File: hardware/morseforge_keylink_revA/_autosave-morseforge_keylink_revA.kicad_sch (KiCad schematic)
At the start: 18 parts, among them J1 USB_C_Receptacle_USB2.0_14P, J2 Conn_01x02_Socket, SW1 SW_SPST, U1 MCP73831-2-MC, U2 LDO40LPU33RY

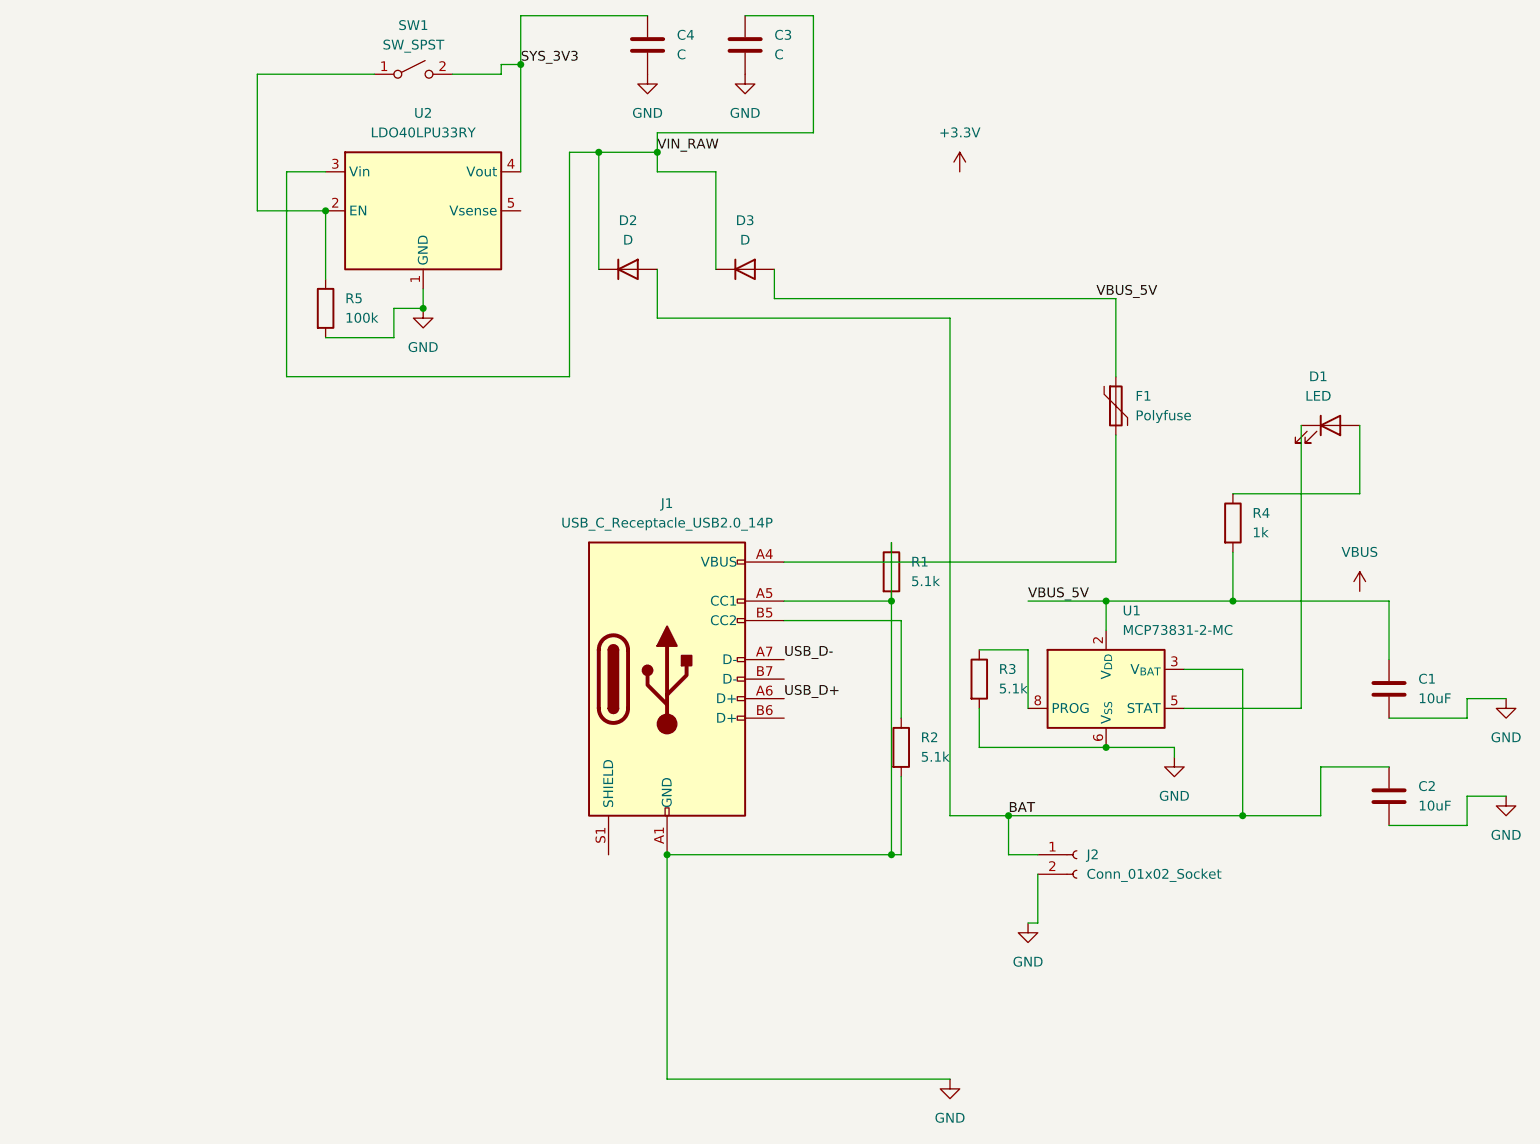
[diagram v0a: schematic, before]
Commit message: USB-UART blocks
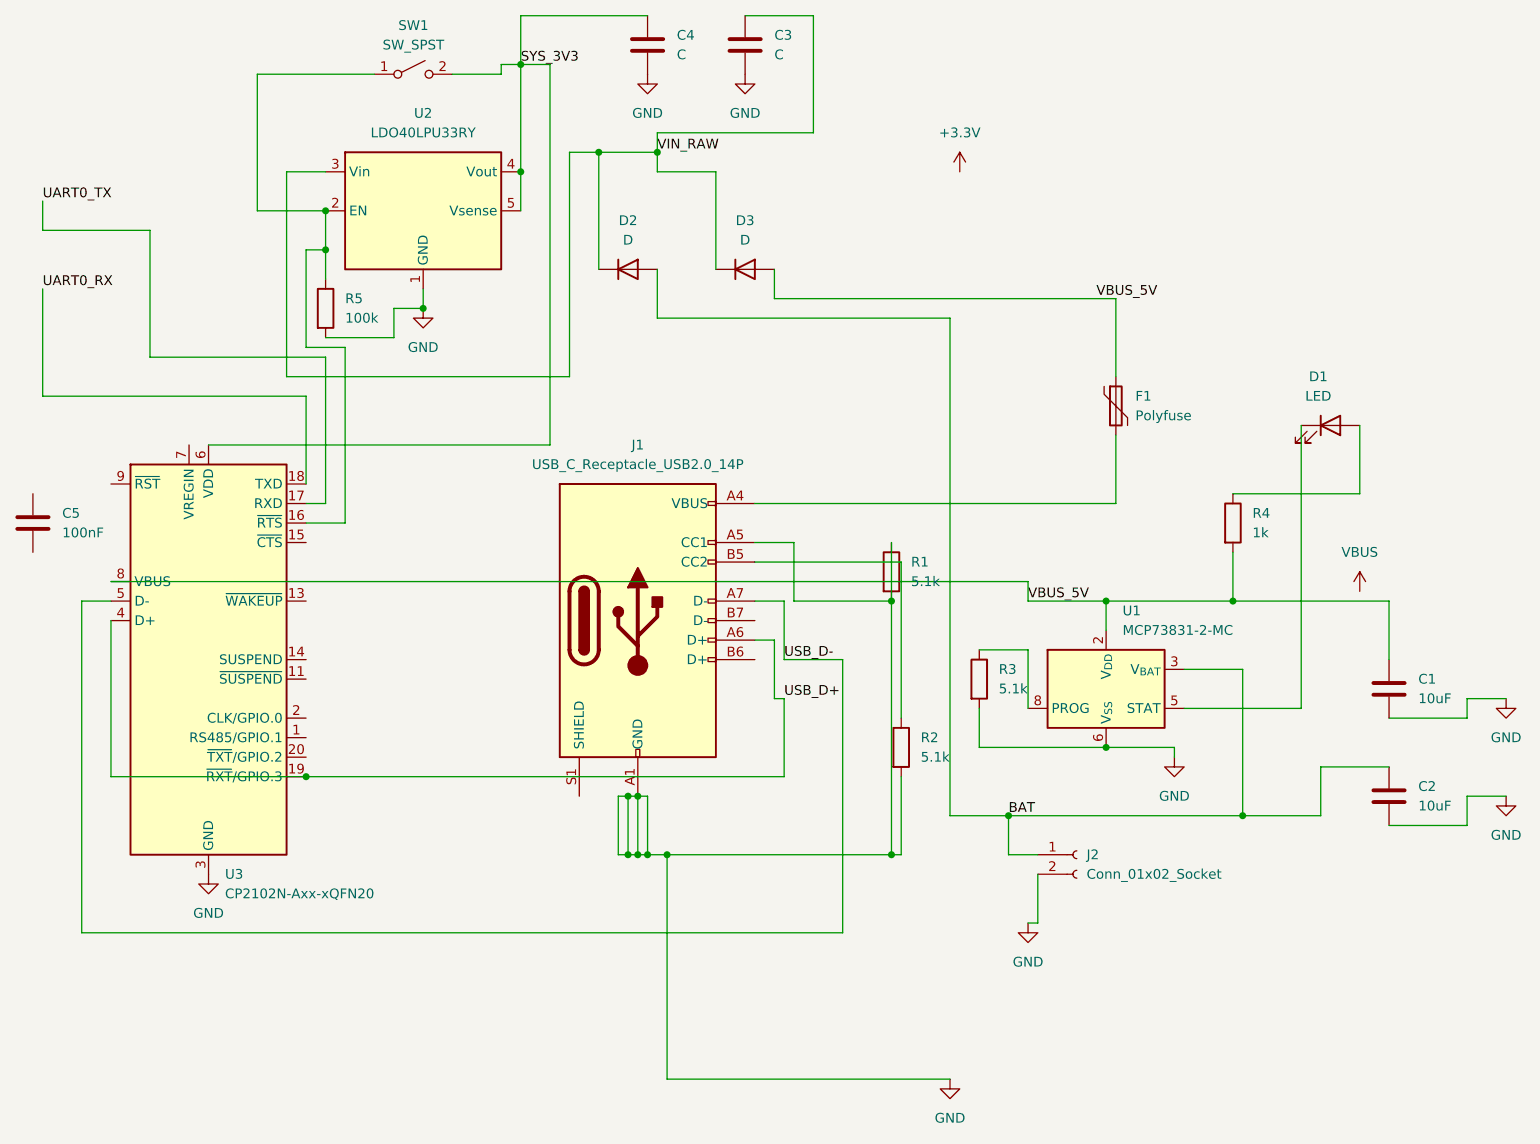
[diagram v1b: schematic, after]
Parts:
- added C5: 100nF, symbol Device:C
- added U3: CP2102N-Axx-xQFN20, Package_DFN_QFN:SiliconLabs_QFN-20-1EP_3x3mm_P0.5mm, symbol Interface_USB:CP2102N-Axx-xQFN20
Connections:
- net GND: now also U3.12 (GND), U3.21 (GND), U3.3 (GND)
- net SYS_3V3: now also U2.5 (Vsense), U3.6 (VDD)
- net USB_D+: now also U3.19 (~{RXT}/GPIO.3), U3.4 (D+)
- net USB_D-: now also U3.5 (D-)
- net VBUS_5V: now also U3.8 (VBUS)
- net at R5.1, SW1.1 (A), U2.2 (EN): now also U3.16 (~{RTS})
- new net UART0_RX: U3.18 (TXD)
- new net UART0_TX: U3.17 (RXD)
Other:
- moved on the sheet: J1
